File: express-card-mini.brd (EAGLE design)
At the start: 11.2 x 65 mm, 1 part

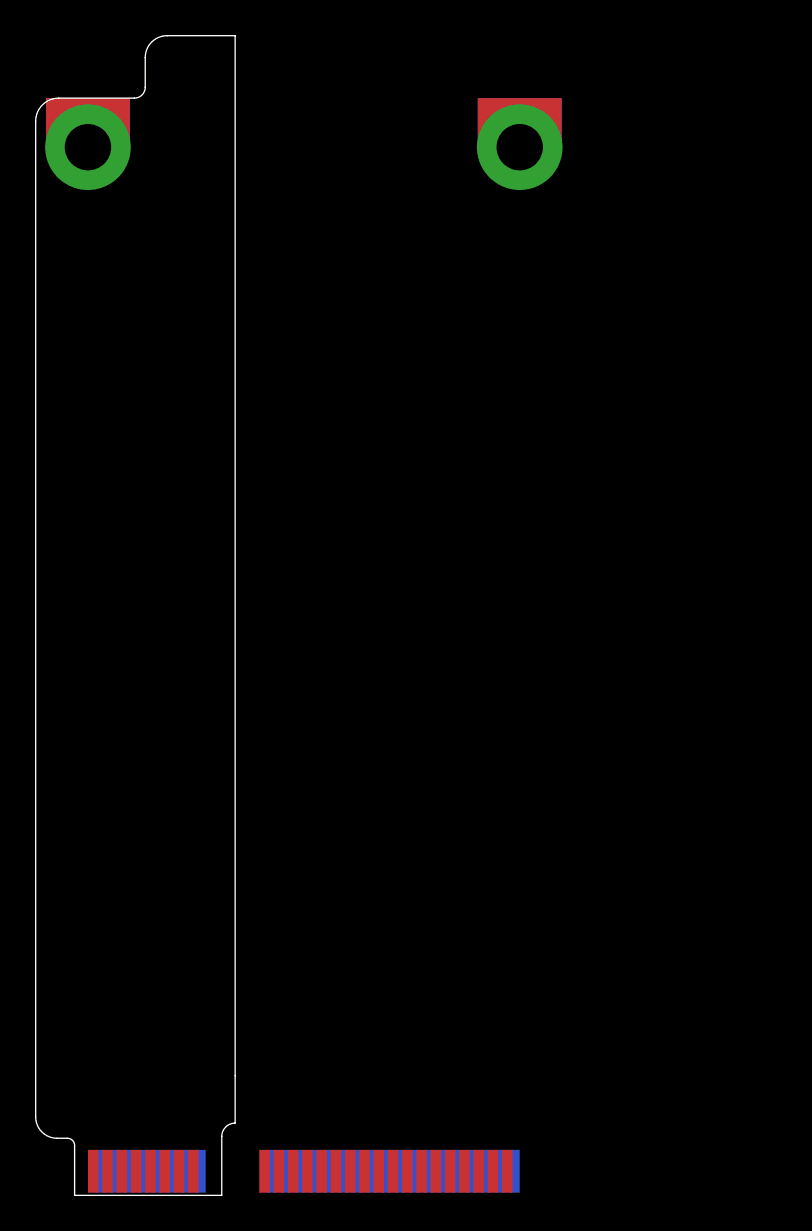
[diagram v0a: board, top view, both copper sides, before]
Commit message: board placement into positive values
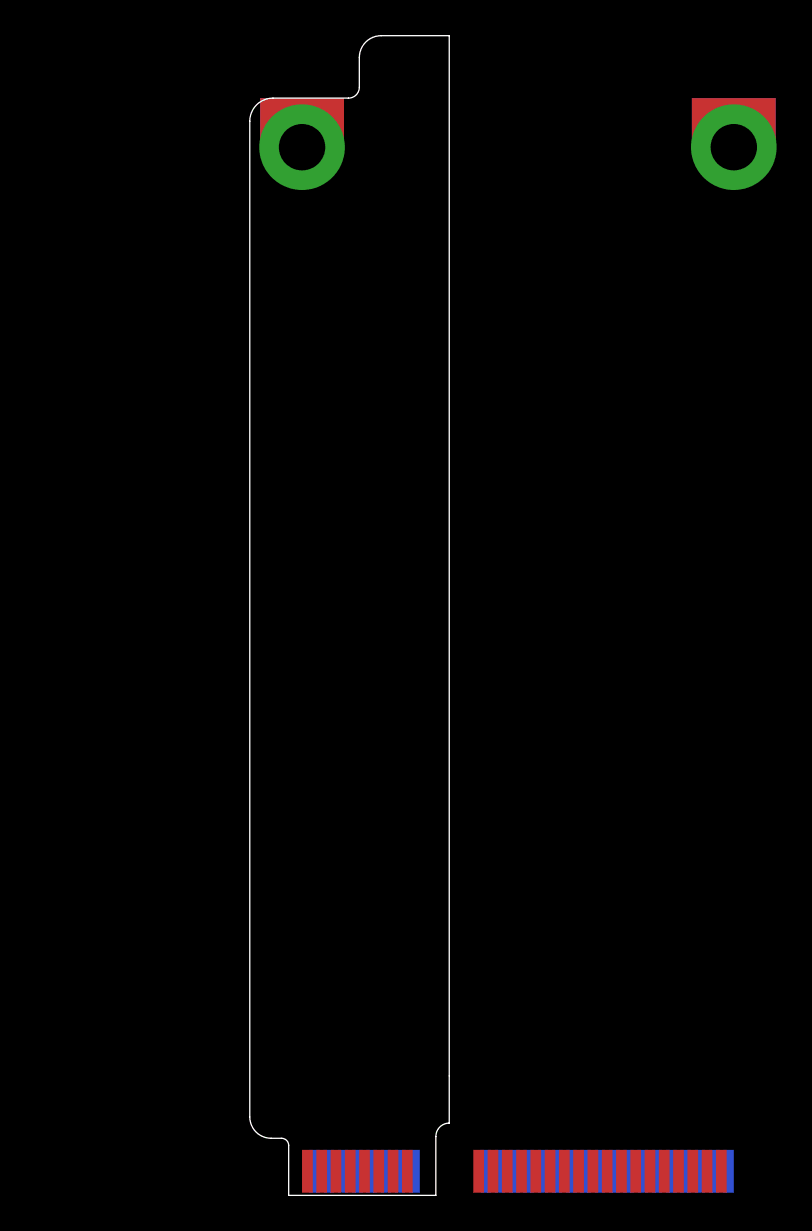
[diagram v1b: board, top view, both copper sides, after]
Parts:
- moved U$1 12.0 mm to (12.0, 0.00)
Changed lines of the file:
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@@
 <setting verticaltext="up"/>
 </settings>
-<grid distance="0.1" unitdist="mm" unit="mm" style="lines" multiple="1" display="yes" altdistance="0.025" altunitdist="inch" altunit="inch"/>
+<grid distance="1" unitdist="mm" unit="mm" style="lines" multiple="1" display="yes" altdistance="0.025" altunitdist="inch" altunit="inch"/>
 <layers>
 <layer number="1" name="Top" color="4" fill="1" visible="yes" active="yes"/>
@@
 <board>
 <plain>
-<wire x1="-0.75" y1="0.1" x2="-0.75" y2="3.4" width="0" layer="20"/>
-<wire x1="-0.75" y1="3.4" x2="0" y2="4.15" width="0" layer="20" curve="-90"/>
-<wire x1="-0.75" y1="0.1" x2="-9" y2="0.1" width="0" layer="20"/>
-<wire x1="-9" y1="0.1" x2="-9" y2="2.9" width="0" layer="20"/>
-<wire x1="-9.4" y1="3.3" x2="-9.983171875" y2="3.3" width="0" layer="20"/>
-<wire x1="-9.983171875" y1="3.3" x2="-11.18" y2="4.496828125" width="0" layer="20" curve="-90"/>
-<wire x1="-11.18" y1="4.496828125" x2="-11.18" y2="60.3067875" width="0" layer="20"/>
-<wire x1="-11.18" y1="60.3067875" x2="-9.8867875" y2="61.6" width="0" layer="20" curve="-90"/>
-<wire x1="-9.8867875" y1="61.6" x2="-5.6495875" y2="61.6" width="0" layer="20"/>
-<wire x1="-9.4" y1="3.3" x2="-9" y2="2.9" width="0" layer="20" curve="-90"/>
-<wire x1="-5.6495875" y1="61.6" x2="-5.04" y2="62.2095875" width="0" layer="20" curve="90"/>
-<wire x1="-5.04" y1="62.2095875" x2="-5.04" y2="63.874603125" width="0" layer="20"/>
-<wire x1="-5.04" y1="63.874603125" x2="-3.814603125" y2="65.1" width="0" layer="20" curve="-90"/>
-<wire x1="-3.814603125" y1="65.1" x2="0" y2="65.1" width="0" layer="20"/>
-<wire x1="0" y1="4.15" x2="0" y2="6.8" width="0" layer="20"/>
-<wire x1="0" y1="6.8" x2="0" y2="65.1" width="0" layer="20"/>
+<wire x1="11.25" y1="0.1" x2="11.25" y2="3.4" width="0" layer="20"/>
+<wire x1="11.25" y1="3.4" x2="12" y2="4.15" width="0" layer="20" curve="-90"/>
+<wire x1="11.25" y1="0.1" x2="3" y2="0.1" width="0" layer="20"/>
+<wire x1="3" y1="0.1" x2="3" y2="2.9" width="0" layer="20"/>
+<wire x1="2.6" y1="3.3" x2="2.016828125" y2="3.3" width="0" layer="20"/>
+<wire x1="2.016828125" y1="3.3" x2="0.82" y2="4.496828125" width="0" layer="20" curve="-90"/>
+<wire x1="0.82" y1="4.496828125" x2="0.82" y2="60.3067875" width="0" layer="20"/>
+<wire x1="0.82" y1="60.3067875" x2="2.1132125" y2="61.6" width="0" layer="20" curve="-90"/>
+<wire x1="2.1132125" y1="61.6" x2="6.3504125" y2="61.6" width="0" layer="20"/>
+<wire x1="2.6" y1="3.3" x2="3" y2="2.9" width="0" layer="20" curve="-90"/>
+<wire x1="6.3504125" y1="61.6" x2="6.96" y2="62.2095875" width="0" layer="20" curve="90"/>
+<wire x1="6.96" y1="62.2095875" x2="6.96" y2="63.874603125" width="0" layer="20"/>
+<wire x1="6.96" y1="63.874603125" x2="8.185396875" y2="65.1" width="0" layer="20" curve="-90"/>
+<wire x1="8.185396875" y1="65.1" x2="12" y2="65.1" width="0" layer="20"/>
+<wire x1="12" y1="4.15" x2="12" y2="6.8" width="0" layer="20"/>
+<wire x1="12" y1="6.8" x2="12" y2="65.1" width="0" layer="20"/>
 </plain>
 <attributes>
@@
 </autorouter>
 <elements>
-<element name="U$1" library="teensy-express" package="FULL-MINI-PCI-E" value="FULL-MINI-PCI-E" x="0" y="0"/>
+<element name="U$1" library="teensy-express" package="FULL-MINI-PCI-E" value="FULL-MINI-PCI-E" x="12" y="0"/>
 </elements>
 <signals>
@@
 <contactref element="U$1" pad="LATCH@1"/>
 <contactref element="U$1" pad="LATCH@2"/>
-<wire x1="-8.25" y1="58.85" x2="15.95" y2="58.85" width="0" layer="19" extent="1-1"/>
+<wire x1="3.75" y1="58.85" x2="27.95" y2="58.85" width="0" layer="19" extent="1-1"/>
 </signal>
 </signals>
